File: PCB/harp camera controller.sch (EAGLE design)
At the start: 113 parts, among them IC1 USBLC6-2SC6, IC10 SI8610BC-B-IS, IC2 74LVC1G240DBV, IC3 74LVC1G240DBV, IC4 FT232RL, IC5 TLV70033DDCR, IC6 ATXMEGA32A4U-AU, IC7 SN74LVC1G125DBVT, IC8 SN74LVC1G125DBVT, IC9 TLV70033DDCR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

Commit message: Updated PCB to version 1.2
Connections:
- net CLOCK_IN: now also IC6.PC2/OC0C/RXD0; no longer IC6.!!RXD1MISOPD6
- net CLOCK_OUT: now also IC6.PC3/OC0D/TXD0; no longer IC6.!!!TXD1SCKCLKOPD7
- net U_IN_CAM2_STROBE_5V: now also IC6.!!!TXD1SCKCLKOPD7; no longer IC6.PC3/OC0D/TXD0
- net U_IN_CAM2_STROBE_PULLUP_5V: now also IC6.!!RXD1MISOPD6; no longer IC6.PC2/OC0C/RXD0
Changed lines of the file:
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@@
 </segment>
 <segment>
-<wire x1="576.58" y1="452.12" x2="604.52" y2="452.12" width="0.1524" layer="91"/>
-<label x="604.52" y="452.12" size="1.778" layer="95" rot="MR0"/>
-<pinref part="IC6" gate="G$1" pin="!!RXD1MISOPD6"/>
+<pinref part="IC6" gate="G$1" pin="PC2/OC0C/RXD0"/>
+<wire x1="459.74" y1="424.18" x2="515.62" y2="424.18" width="0.1524" layer="91"/>
+<label x="459.74" y="424.18" size="1.778" layer="95"/>
 </segment>
 </net>
@@
 </segment>
 <segment>
-<wire x1="576.58" y1="449.58" x2="604.52" y2="449.58" width="0.1524" layer="91"/>
-<label x="604.52" y="449.58" size="1.778" layer="95" rot="MR0"/>
-<pinref part="IC6" gate="G$1" pin="!!!TXD1SCKCLKOPD7"/>
+<pinref part="IC6" gate="G$1" pin="PC3/OC0D/TXD0"/>
+<wire x1="515.62" y1="421.64" x2="459.74" y2="421.64" width="0.1524" layer="91"/>
+<label x="459.74" y="421.64" size="1.778" layer="95"/>
 </segment>
 </net>
@@
 </segment>
 <segment>
-<wire x1="459.74" y1="421.64" x2="515.62" y2="421.64" width="0.1524" layer="91"/>
-<label x="459.74" y="421.64" size="1.778" layer="95"/>
-<pinref part="IC6" gate="G$1" pin="PC3/OC0D/TXD0"/>
+<wire x1="576.58" y1="449.58" x2="629.92" y2="449.58" width="0.1524" layer="91"/>
+<pinref part="IC6" gate="G$1" pin="!!!TXD1SCKCLKOPD7"/>
+<label x="629.92" y="449.58" size="1.778" layer="95" rot="MR0"/>
 </segment>
 </net>
@@
 </segment>
 <segment>
-<wire x1="459.74" y1="424.18" x2="515.62" y2="424.18" width="0.1524" layer="91"/>
-<label x="459.74" y="424.18" size="1.778" layer="95"/>
-<pinref part="IC6" gate="G$1" pin="PC2/OC0C/RXD0"/>
-</segment>
-</net>
+<wire x1="576.58" y1="452.12" x2="629.92" y2="452.12" width="0.1524" layer="91"/>
+<pinref part="IC6" gate="G$1" pin="!!RXD1MISOPD6"/>
+<label x="629.92" y="452.12" size="1.778" layer="95" rot="MR0"/>
+</segment>
+</net>

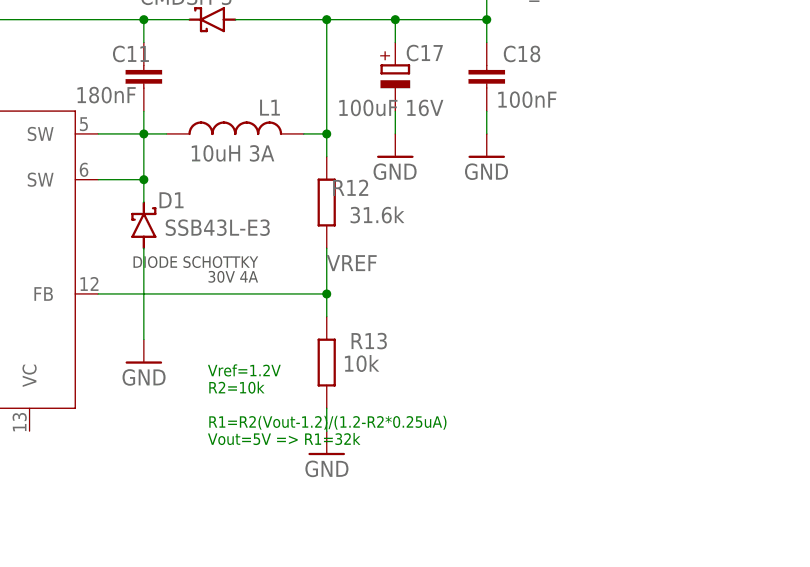
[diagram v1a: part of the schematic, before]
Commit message: Changed 5V output to 5.3V and released PCB v1.2
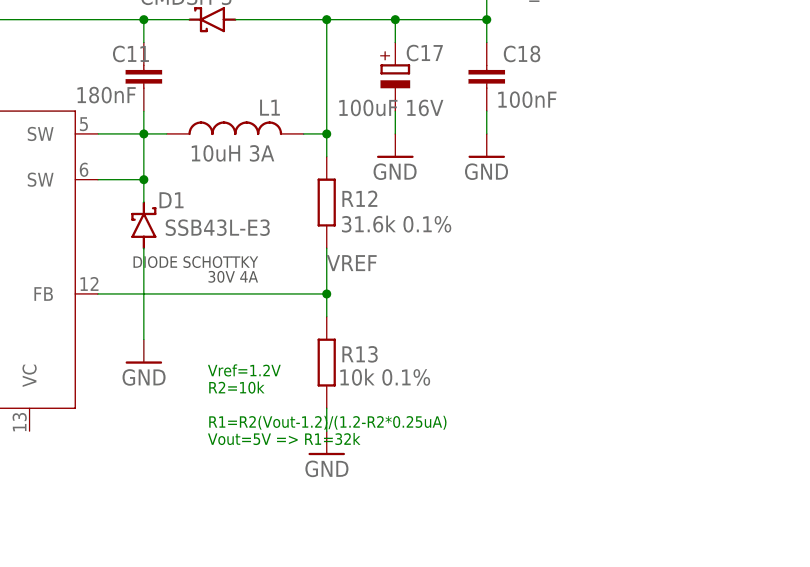
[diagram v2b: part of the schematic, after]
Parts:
- R12: value 31.6k -> 31.6k 0.1%
- R13: value 10k -> 10k 0.1%
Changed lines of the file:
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@@
 <attribute name="TYPE" value="SMD"/>
 </part>
-<part name="R12" library="rcl" deviceset="R-EU_" device="R0402" value="31.6k">
+<part name="R12" library="rcl" deviceset="R-EU_" device="R0402" value="31.6k 0.1%">
 <attribute name="DIGIKEY_PN" value="311-40.2KLRCT-ND"/>
 <attribute name="MPN" value="RC0402FR-0740K2L"/>
 <attribute name="TYPE" value="SMD"/>
 </part>
-<part name="R13" library="rcl" deviceset="R-EU_" device="R0402" value="10k">
+<part name="R13" library="rcl" deviceset="R-EU_" device="R0402" value="10k 0.1%">
 <attribute name="DIGIKEY_PN" value="541-3959-1-ND"/>
 <attribute name="MPN" value="CRCW040210K0FKED"/>
@@
 </instance>
 <instance part="R12" gate="G$1" x="154.94" y="467.36" smashed="yes" rot="MR90">
-<attribute name="NAME" x="159.766" y="468.0966" size="1.778" layer="95" rot="MR0"/>
-<attribute name="VALUE" x="163.576" y="465.074" size="1.778" layer="96" rot="MR0"/>
+<attribute name="NAME" x="156.464" y="468.6554" size="1.778" layer="95" rot="MR180"/>
+<attribute name="VALUE" x="156.464" y="465.836" size="1.778" layer="96" rot="MR180"/>
 <attribute name="MPN" x="154.94" y="467.36" size="1.778" layer="96" rot="MR90" display="off"/>
 <attribute name="TYPE" x="154.94" y="467.36" size="1.778" layer="96" rot="MR90" display="off"/>
@@
 </instance>
 <instance part="R13" gate="G$1" x="154.94" y="449.58" smashed="yes" rot="MR90">
-<attribute name="NAME" x="161.798" y="451.0786" size="1.778" layer="95" rot="MR0"/>
-<attribute name="VALUE" x="160.782" y="448.564" size="1.778" layer="96" rot="MR0"/>
+<attribute name="NAME" x="156.464" y="451.3834" size="1.778" layer="95" rot="MR180"/>
+<attribute name="VALUE" x="156.21" y="448.818" size="1.778" layer="96" rot="MR180"/>
 <attribute name="MPN" x="154.94" y="449.58" size="1.778" layer="96" rot="MR90" display="off"/>
 <attribute name="TYPE" x="154.94" y="449.58" size="1.778" layer="96" rot="MR90" display="off"/>
